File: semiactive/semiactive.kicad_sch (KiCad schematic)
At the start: 1 part

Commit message: Setup libs, scripts
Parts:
- removed U?: Teensy4.1, symbol teensy:Teensy4.1
- added C1: (no value), symbol Device:C
- added C2, C3: C, symbol Device:C
- added D1, D2, D3: (no value), symbol IN-PI42TASPRPGPB:IN-PI42TASPRPGPB
- added D4, D5, D6: (no value), symbol LED:WS2812B
- added J4: 5223002-2, symbol semiactive-altium-import:0_mirrored_5223002-2
- added U1: Teensy4.1, symbol teensy:Teensy4.1
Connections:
- new net: D2.3 (DOUT), D3.1 (DIN)
- new net: D4.2 (DOUT), D5.4 (DIN)
- new net: D1.3 (DOUT), D2.1 (DIN)
- new net: D5.2 (DOUT), D6.4 (DIN)
- new net 3.3V: J4.7, J4.8, J4.9
- new net 5V: C1.1, C2.1, C3.1, D1.2 (VDD), D2.2 (VDD), D3.2 (VDD), D4.1 (VDD), D5.1 (VDD), D6.1 (VDD), J4.4, J4.5, J4.6, U1.48 (VIN)
- new net 8.4V: J4.1, J4.2, J4.3
- new net ARGBLED: D1.1 (DIN), D4.4 (DIN), U1.7 (5_IN2)
- new net CAN_H: J4.20
- new net CAN_L: J4.21
- new net CIPO: J4.17
- new net COPI: J4.18
- new net DIG_OUT: J4.24
- new net DIR1: J4.45
- new net DIR2: J4.46
- new net ENGHALL1: J4.26
- new net ENGHALL2: J4.38
- new net FRBPRESS: J4.47
- new net GND: C1.2, C2.2, C3.2, D1.4 (GND), D2.4 (GND), D3.4 (GND), D4.3 (VSS), D5.3 (VSS), D6.3 (VSS), J4.10, J4.11, J4.12, U1.1 (GND), U1.34 (GND), U1.47 (GND), U1.52 (GND), U1.58 (GND), U1.59 (GND)
- new net I2C_CLK: J4.14
- new net I2C_DATA: J4.13
- new net IR_AMP: J4.35
- new net IR_TEENSY: J4.36
- new net N_A: J4.37
- new net PENC_A: J4.49
- new net PENC_B: J4.51
- new net PLDCLK: J4.57
- new net PLDDAT: J4.58
- new net PLOADC1: J4.41
- new net PLOADC2: J4.42
- new net PWM1: J4.43
- new net PWM2: J4.44
- new net RPOT1: J4.22
- new net RPOT2: J4.23
- new net RRBPRESS: J4.48
- new net RRHALL: J4.25
- new net RX: J4.16, U1.10 (8_TX2_IN1)
- new net SCLK: J4.19
- new net SENC_A: J4.53
- new net SENC_B: J4.55
- new net SLDCLK: J4.59
- new net SLDDAT: J4.60
- new net SLOADC1: J4.39
- new net SLOADC2: J4.40
- new net SPARK: J4.27
- new net TEMP1: J4.28
- new net TEMP2: J4.29
- new net TEMP3: J4.30
- new net TEMP4: J4.31
- new net TX: J4.15, U1.9 (7_RX2_OUT1A)
- new net VOLT1: J4.32, U1.5 (3_LRCLK2)
- new net VOLT2: J4.33, U1.6 (4_BCLK2)
- new net VOLT3: J4.34
- new net ~PENC_A: J4.50
- new net ~PENC_B: J4.52
- new net ~SENC_A: J4.54
- new net ~SENC_B: J4.56
- no-connect marks 0 -> 56
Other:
- note added: "LEDs"
- note added: "LEDs (Backup)"

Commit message: Create a few projects
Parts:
- C1: value (none) -> C; footprint (none) -> Capacitor_SMD:C_0603_1608Metric
- C2, C3: footprint (none) -> Capacitor_SMD:C_0603_1608Metric
- D1: value (none) -> SET.F; footprint (none) -> !footprints:LED_IN-PI42TASPRPGPB
- D2: value (none) -> SET.R; footprint (none) -> !footprints:LED_IN-PI42TASPRPGPB
- D3: value (none) -> STATUS; footprint (none) -> !footprints:LED_IN-PI42TASPRPGPB
- D4: value (none) -> SET.F; footprint (none) -> !footprints:LED_WS2812B_PLCC4_5.0x5.0mm_P3.2mm
- D5: value (none) -> SET.R; footprint (none) -> !footprints:LED_WS2812B_PLCC4_5.0x5.0mm_P3.2mm
- D6: value (none) -> STATUS; footprint (none) -> !footprints:LED_WS2812B_PLCC4_5.0x5.0mm_P3.2mm
- J4: footprint (none) -> !footprints:52230042
- U1: footprint (none) -> !footprints:Teensy41
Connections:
- no-connect marks 56 -> 57
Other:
- moved on the sheet: D4, D5, D6

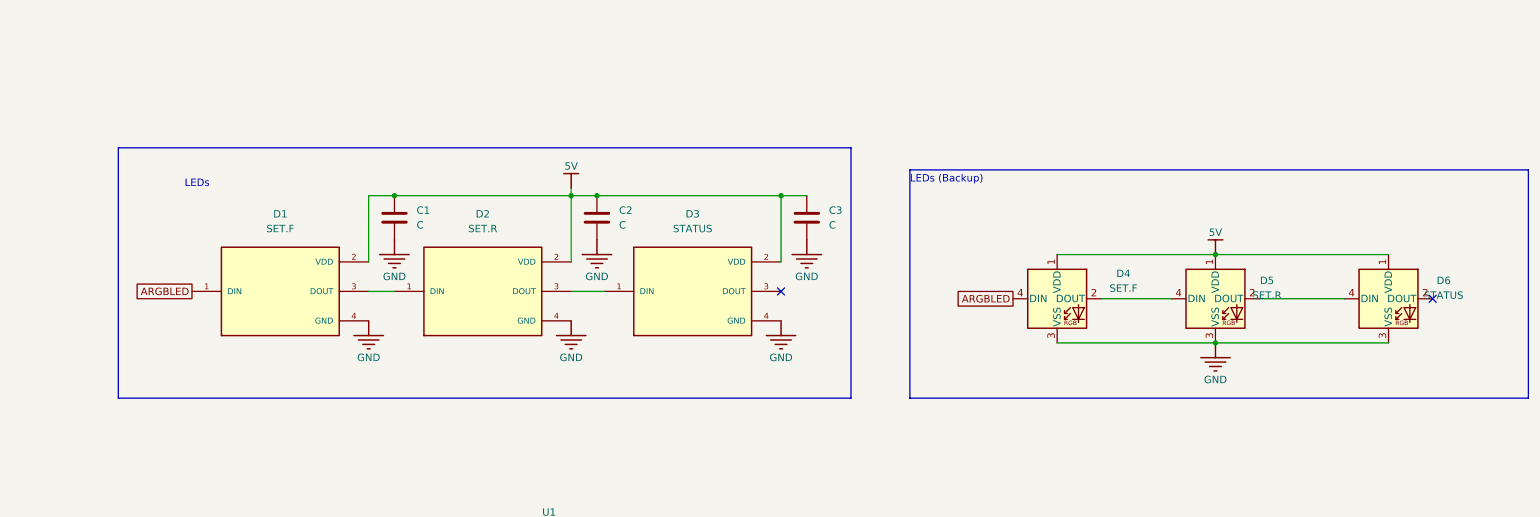
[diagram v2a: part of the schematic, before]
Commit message: Route SAS board
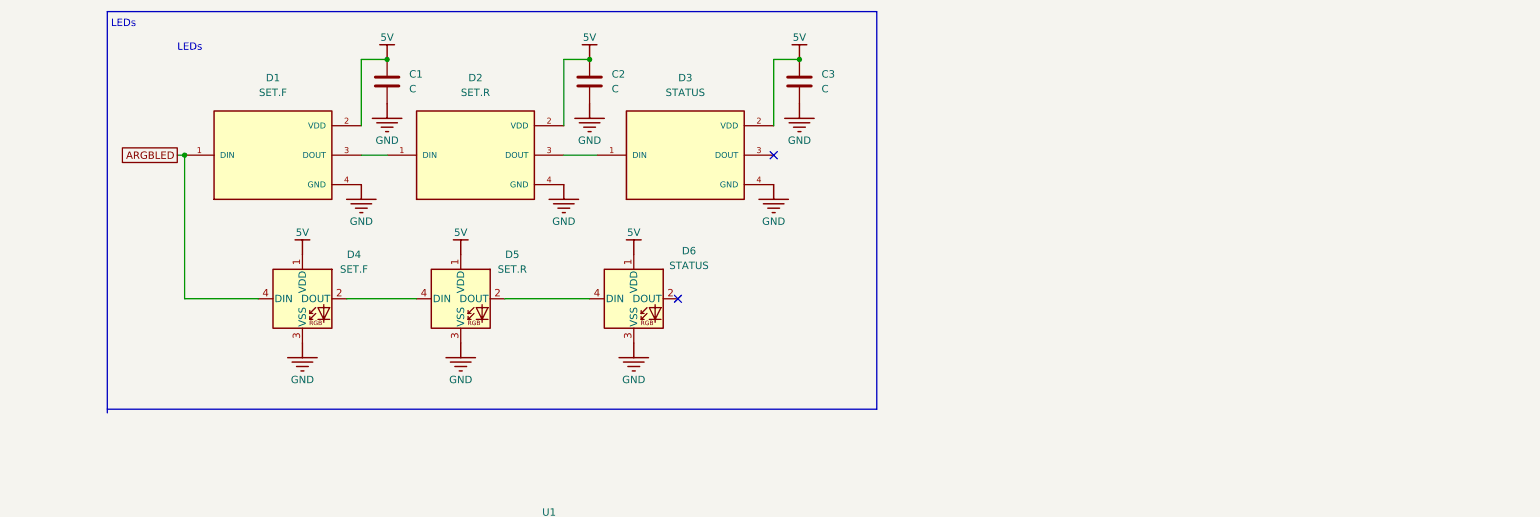
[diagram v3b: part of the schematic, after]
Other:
- note removed: "LEDs (Backup)"
- moved on the sheet: C1, C2, C3, D1, D2, D3, D4, D5, D6

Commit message: Easter eggs
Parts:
- removed J4: 5223002-2, !footprints:52230042, symbol semiactive-altium-import:0_mirrored_5223002-2
- added J1: 5223004-2, !footprints:52230042, symbol semiactive-altium-import:root_0_5223004-2
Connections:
- net 5V: now also J1.E4, J1.E5, J1.E6
- net CIPO: now also J1.D5
- net COPI: now also J1.D6
- net DIG_OUT: now also J1.D12
- net GND: now also J1.E10, J1.E11, J1.E12
- net PWM1: now also J1.B7
- net PWM2: now also J1.B8
- net RPOT1: now also J1.D10
- net RPOT2: now also J1.D11
- net RX renamed CVT_RX_DAQ_TX
- net CVT_RX_DAQ_TX: now also J1.D4
- net TX renamed CVT_TX_DAQ_RX
- net CVT_TX_DAQ_RX: now also J1.D3
- net VOLT1 renamed SOLENOID_PWM_1
- net SOLENOID_PWM_1: now also J1.C9
- net VOLT2 renamed SOLENOID_PWM_2
- net SOLENOID_PWM_2: now also J1.C10
- new net +3V3: J1.E7, J1.E8, J1.E9
- new net 36V_SENS: J1.C8
- new net CANH: J1.D8
- new net CANL: J1.D9
- new net DIRECTION1: J1.B9
- new net DIRECTION2: J1.B10
- new net ENG_HALL1_IN: J1.C2
- new net ENG_HALL2_IN: J1.B2
- new net FBREAK_PRESSURE_IN: J1.B11
- new net IR_SENS_TNC: J1.C12
- new net PENC_CHA: J1.A1
- new net PENC_CHA/: J1.A2
- new net PENC_CHB/: J1.A4
- new net PENc_CHB: J1.A3
- new net PLOAD_CELL_CLK: J1.A9
- new net PLOAD_CELL_DATA: J1.A10
- new net RBREAK_PRESSURE_IN: J1.B12
- new net REAR_HALL_IN: J1.C1
- new net SCL: J1.D2
- new net SDA: J1.D1
- new net SENC_CHA: J1.A5
- new net SENC_CHA/: J1.A6
- new net SENC_CHB: J1.A7
- new net SENC_CHB/: J1.A8
- new net SLOAD_CELL_CLK: J1.A11
- new net SLOAD_CELL_DATA: J1.A12
- new net SPI_CLK: J1.D7
- new net SPK_PLUG: J1.C3
- new net THERM_SENS1: J1.C4
- new net THERM_SENS2: J1.C5
- new net THERM_SENS3: J1.C6
- new net THERM_SENS4: J1.C7
- no-connect marks 57 -> 66

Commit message: Semiactive, DAQ-wireless updates (schem, board)
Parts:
- added D7: D, symbol Device:D
- C1, C2, C3: value C -> 1uF
- D4, D5, D6: now not fitted
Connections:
- net 5V: now also D7.1 (K); no longer U1.48 (VIN)
- new net: D7.2 (A), U1.48 (VIN)

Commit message: BOM
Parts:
- D7: footprint (none) -> Diode_SMD:D_SMA
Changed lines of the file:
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@@
       (effects (font (size 1.27 1.27)) (justify left))
     )
-    (property "Footprint" "" (at 229.235 99.695 0)
+    (property "Footprint" "Diode_SMD:D_SMA" (at 229.235 99.695 0)
       (effects (font (size 1.27 1.27)) hide)
     )
